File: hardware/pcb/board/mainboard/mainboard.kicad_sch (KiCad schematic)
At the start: 137 parts, among them J1 Conn_Coaxial, J10 USB_C_Receptacle, J11 2908-05WB-MG, J3 Conn_02x35_Odd_Even_MountingP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, J4 Conn_02x40_Odd_Even_MountingP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, J5 Conn_02x40_Odd_Even_MountingP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, J6 USB_C_Receptacle, J7 Conn_01x30, J8 Conn_01x30, J9 Conn_01x30, Q1 BSS138, Q2 DMN3008SFG, Q3 DMN3008SFG, U1 TPS7A20_SOT-23, U11 TPS7A20_SOT-23, U12 AP33771C, U13 TXS0104E, U14 FT234XD-R, U2 LSM6DS3TR, U3 NEO-M8N, U4 BQ25606, U5 BQ27441-G1, U6 SN74LVC1T45DBVR, U7 LIS2MDL, U8 SN74LVC1T45DBVR, U9 TPS61235P

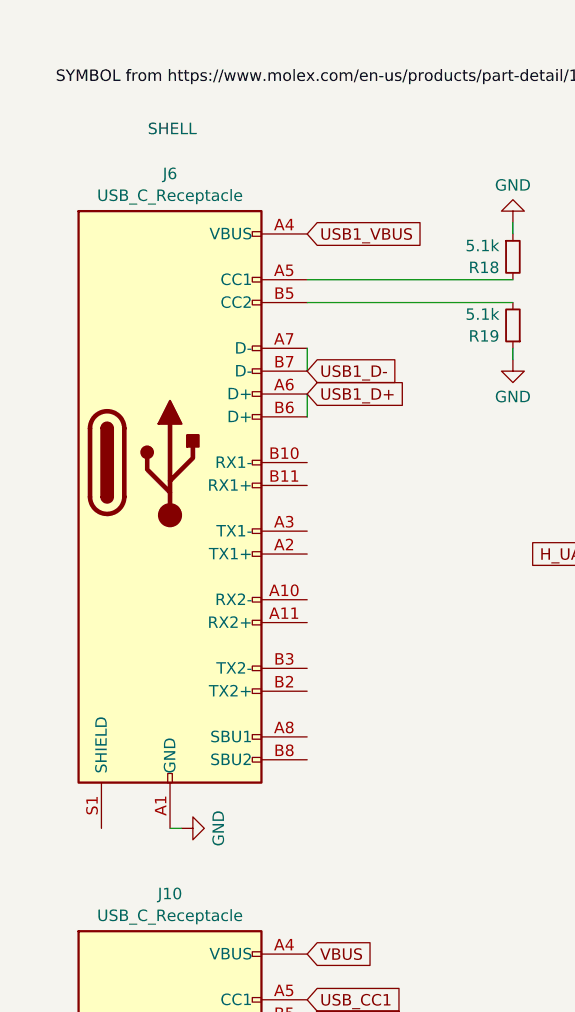
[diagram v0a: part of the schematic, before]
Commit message: switch to vertical USB C receptable for shell
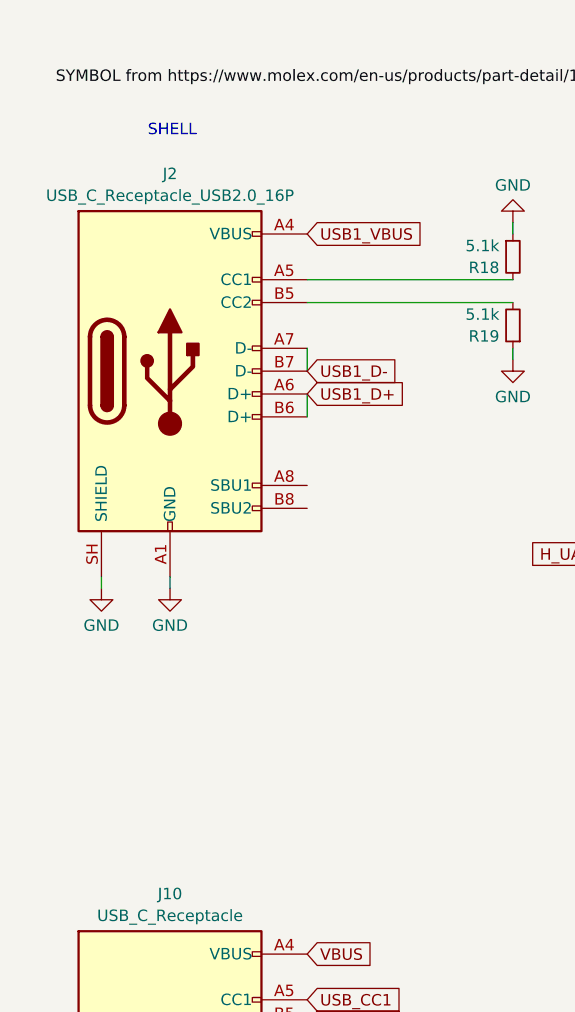
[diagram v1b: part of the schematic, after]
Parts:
- removed J6: USB_C_Receptacle, Connector_USB:USB_C_CONN_1054550101_MOL, symbol Connector:USB_C_Receptacle
- added J2: USB_C_Receptacle_USB2.0_16P, unsurv_offline_pcb_footprints:2171820001_USB_C_MOLEX, symbol Connector:USB_C_Receptacle_USB2.0_16P
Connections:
- net GND: now also J2.A1 (GND), J2.A12 (GND), J2.B1 (GND), J2.B12 (GND), J2.SH (SHIELD)
- net USB1_D+: now also J2.A6 (D+), J2.B6 (D+)
- net USB1_D-: now also J2.A7 (D-), J2.B7 (D-)
- net USB1_VBUS: now also J2.A4 (VBUS), J2.A9 (VBUS), J2.B4 (VBUS), J2.B9 (VBUS)
- net at R19.2: now also J2.B5 (CC2)
- net at R18.2: now also J2.A5 (CC1)
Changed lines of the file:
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@@
 	(wire
 		(pts
+			(xy 31.75 279.4) (xy 31.75 280.67)
+		)
+		(stroke
+			(width 0)
+			(type default)
+		)
+	)
+	(wire
+		(pts
 			(xy 551.18 237.49) (xy 553.72 237.49)
 		)
@@
 	(wire
 		(pts
-			(xy 31.75 307.34) (xy 33.02 307.34)
+			(xy 24.13 279.4) (xy 24.13 280.67)
 		)
 		(stroke
@@
 	)
 	(symbol
-		(lib_id "Connector:USB_C_Receptacle")
-		(at 31.75 266.7 0)
+		(lib_id "Connector:USB_C_Receptacle_USB2.0_16P")
+		(at 31.75 256.54 0)
 		(unit 1)
 		(body_style 1)
@@
 		(dnp no)
 		(fields_autoplaced yes)
-		(property "Reference" "J6"
+		(property "Reference" "J2"
 			(at 31.75 234.6155 0)
 			(show_name no)
@@
 			)
 		)
-		(property "Value" "USB_C_Receptacle"
+		(property "Value" "USB_C_Receptacle_USB2.0_16P"
 			(at 31.75 237.0398 0)
 			(show_name no)
@@
 			)
 		)
-		(property "Footprint" "Connector_USB:USB_C_CONN_1054550101_MOL"
-			(at 35.56 266.7 0)
+		(property "Footprint" "unsurv_offline_pcb_footprints:2171820001_USB_C_MOLEX"
+			(at 35.56 256.54 0)
 			(hide yes)
 			(show_name no)
@@
 		)
 		(property "Datasheet" "https://www.usb.org/sites/default/files/documents/usb_type-c.zip"
-			(at 35.56 266.7 0)
+			(at 35.56 256.54 0)
 			(hide yes)
 			(show_name no)
@@
 			)
 		)
-		(property "Description" "USB Full-Featured Type-C Receptacle connector"
-			(at 31.75 266.7 0)
+		(property "Description" "USB 2.0-only 16P Type-C Receptacle connector"
+			(at 31.75 256.54 0)
 			(hide yes)
 			(show_name no)
@@
 			)
 		)
-		(pin "A5"
-		)
-		(pin "A8"
-		)
-		(pin "B12"
-		)
-		(pin "B1"
+		(pin "A1"
 		)
-		(pin "B3"
+		(pin "A4"
 		)
-		(pin "B8"
+		(pin "A6"
 		)
-		(pin "A4"
+		(pin "B5"
 		)
-		(pin "A2"
+		(pin "B6"
 		)
 		(pin "A7"
 		)
-		(pin "A11"
-		)
-		(pin "A3"
+		(pin "B4"
 		)
-		(pin "B10"
+		(pin "A8"
 		)
-		(pin "B11"
+		(pin "B1"
 		)
-		(pin "A12"
+		(pin "B7"
 		)
 		(pin "B9"
 		)
-		(pin "S1"
-		)
-		(pin "A10"
-		)
-		(pin "B6"
+		(pin "B12"
 		)
-		(pin "A1"
+		(pin "A12"
 		)
-		(pin "B5"
+		(pin "A5"
 		)
 		(pin "A9"
 		)
-		(pin "B2"
-		)
-		(pin "A6"
-		)
-		(pin "B4"
+		(pin "B8"
 		)
-		(pin "B7"
+		(pin "SH"
 		)
 		(instances
 			(project "mainboard"
 				(path "/0d10df44-32de-4e15-8354-02c97578c850"
-					(reference "J6")
+					(reference "J2")
 					(unit 1)
 				)
@@
 	(symbol
 		(lib_id "power:GND")
-		(at 33.02 307.34 90)
+		(at 24.13 280.67 0)
 		(unit 1)
 		(body_style 1)
@@
 		(fields_autoplaced yes)
 		(property "Reference" "#PWR0114"
-			(at 39.37 307.34 0)
+			(at 24.13 287.02 0)
 			(hide yes)
 			(show_name no)
@@
 		)
 		(property "Value" "GND"
-			(at 37.1531 307.34 0)
+			(at 24.13 284.8031 0)
 			(show_name no)
 			(do_not_autoplace no)
@@
 		)
 		(property "Footprint" ""
-			(at 33.02 307.34 0)
+			(at 24.13 280.67 0)
 			(hide yes)
 			(show_name no)
@@
 		)
 		(property "Datasheet" ""
-			(at 33.02 307.34 0)
+			(at 24.13 280.67 0)
 			(hide yes)
 			(show_name no)
@@
 		)
 		(property "Description" "Power symbol creates a global label with name \"GND\" , ground"
-			(at 33.02 307.34 0)
+			(at 24.13 280.67 0)
 			(hide yes)
 			(show_name no)
@@
 					(unit 1)
 				)
+			)
+		)
+	)
+	(symbol
+		(lib_id "power:GND")
+		(at 31.75 280.67 0)
+		(unit 1)
+		(body_style 1)
+		(exclude_from_sim no)
+		(in_bom yes)
+		(on_board yes)
+		(in_pos_files yes)
+		(dnp no)
+		(fields_autoplaced yes)
+		(property "Reference" "#PWR0150"
+			(at 31.75 287.02 0)
+			(hide yes)
+			(show_name no)
+			(do_not_autoplace no)
+			(effects
+				(font
+					(size 1.27 1.27)
+				)
+			)
+		)
+		(property "Value" "GND"
+			(at 31.75 284.8031 0)
+			(show_name no)
+			(do_not_autoplace no)
+			(effects
+				(font
+					(size 1.27 1.27)
+				)
+			)
+		)
+		(property "Footprint" ""
+			(at 31.75 280.67 0)
+			(hide yes)
+			(show_name no)
+			(do_not_autoplace no)
+			(effects
+				(font
+					(size 1.27 1.27)
+				)
+			)
+		)
+		(property "Datasheet" ""
+			(at 31.75 280.67 0)
+			(hide yes)
+			(show_name no)
+			(do_not_autoplace no)
+			(effects
+				(font
+					(size 1.27 1.27)
+				)
+			)
+		)
+		(property "Description" "Power symbol creates a global label with name \"GND\" , ground"
+			(at 31.75 280.67 0)
+			(hide yes)
+			(show_name no)
+			(do_not_autoplace no)
+			(effects
+				(font
+					(size 1.27 1.27)
+				)
+			)
+		)
+		(pin "1"
+		)
+		(instances
+			(project "mainboard"
+				(path "/0d10df44-32de-4e15-8354-02c97578c850"
+					(reference "#PWR0150")
+					(unit 1)
+				)

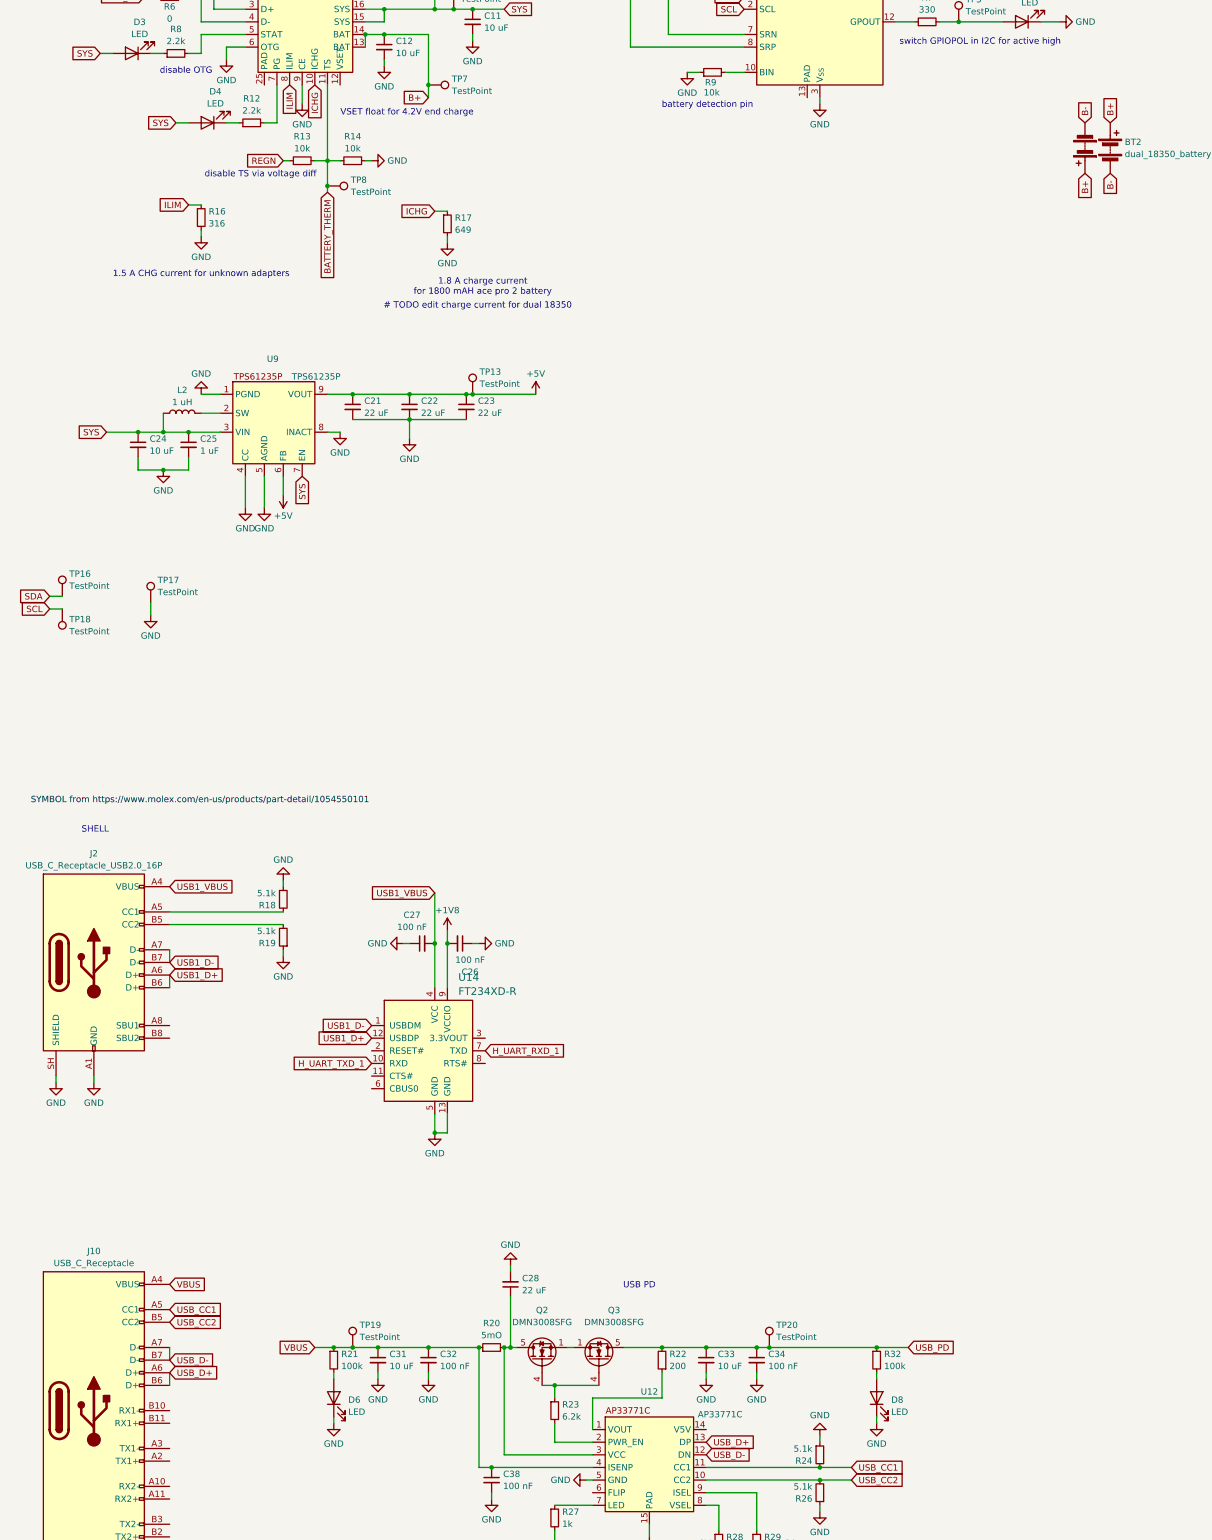
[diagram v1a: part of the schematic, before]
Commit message: BQ25606 routing
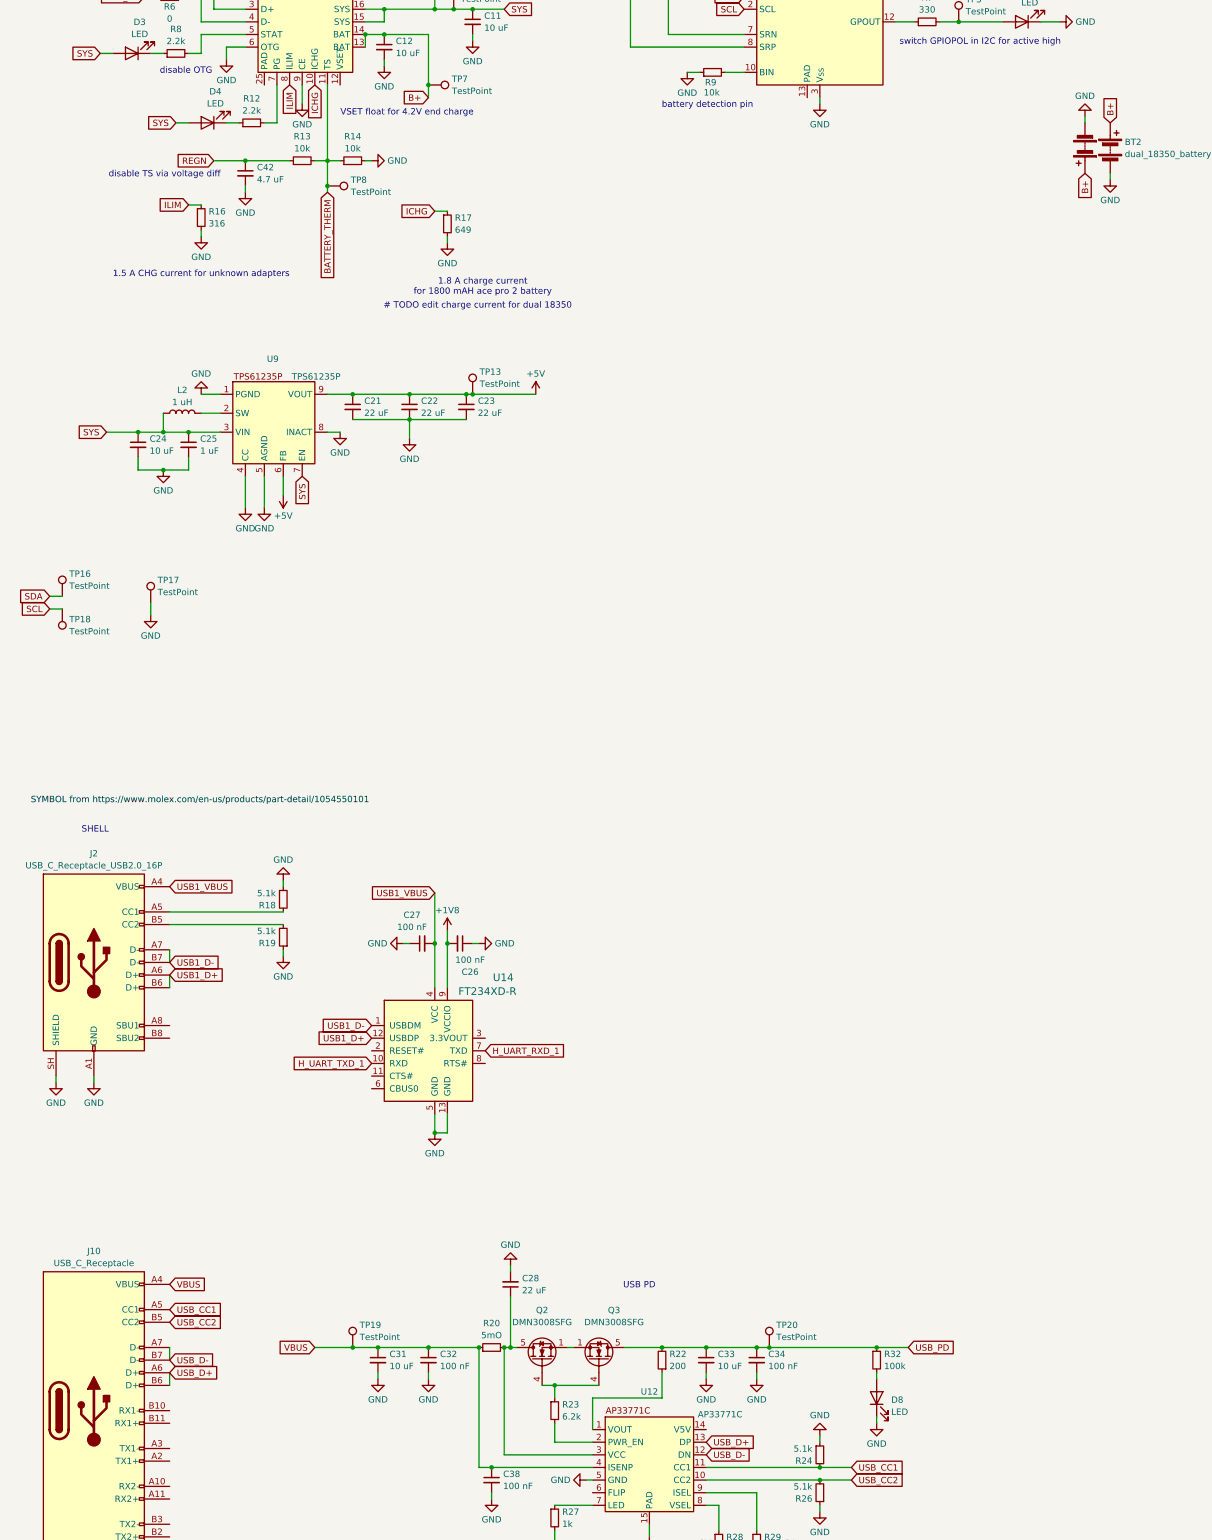
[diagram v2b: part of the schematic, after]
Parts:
- removed D6: LED, LED_SMD:LED_0603_1608Metric, symbol Device:LED
- removed R21: 100k, Resistor_SMD:R_0603_1608Metric, symbol Device:R_Small
- added C42: 4.7 uF, Capacitor_SMD:C_0603_1608Metric, symbol Device:C_Small
- L1: footprint Inductor_SMD:L_0603_1608Metric -> unsurv_offline_pcb_footprints:Inductor_Wuerth_74437321010; MFN (none) -> Wuerth_74437321010
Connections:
- net B- is gone; now on net GND: BT2.2 (-)
- net GND: now also C42.2
- net REGN: now also C42.1

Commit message: TPS61235p 5v PWR routing
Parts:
- L2: footprint Inductor_SMD:L_0603_1608Metric -> Inductor_SMD:L_Coilcraft_XAL5020-XXX; MFN SPM6530T-1R0M120 -> EXLA1V0703-1R0-R
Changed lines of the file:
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@@
 			)
 		)
-		(property "Footprint" "Inductor_SMD:L_0603_1608Metric"
+		(property "Footprint" "Inductor_SMD:L_Coilcraft_XAL5020-XXX"
 			(at 49.53 146.05 0)
 			(hide yes)
@@
 			)
 		)
-		(property "MFN" "SPM6530T-1R0M120"
+		(property "MFN" "EXLA1V0703-1R0-R"
 			(at 49.53 146.05 90)
 			(hide yes)

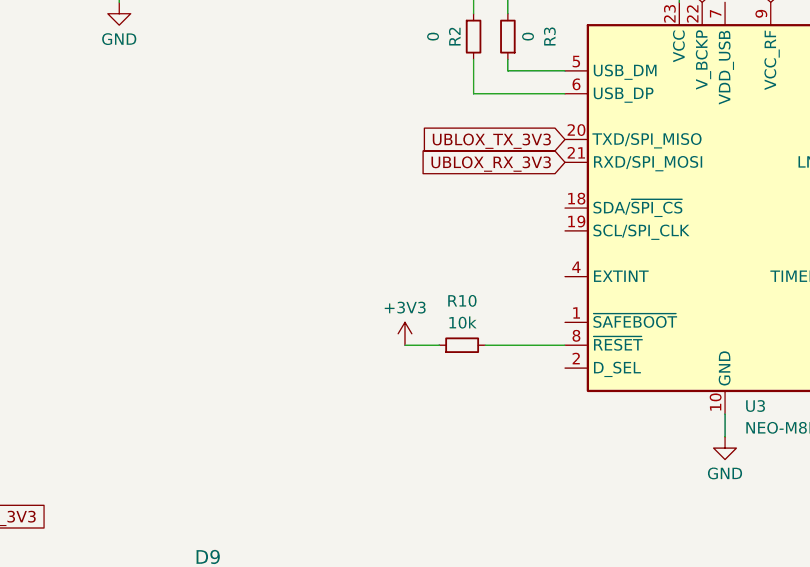
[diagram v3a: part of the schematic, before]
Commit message: route ublox GNSS receiver
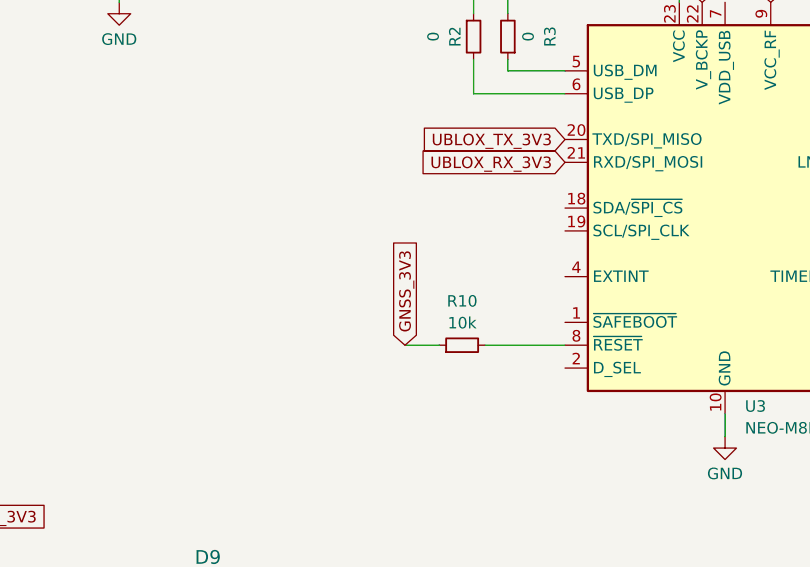
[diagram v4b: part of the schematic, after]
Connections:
- net +3V3: no longer R10.1
- net GNSS_3V3: now also R10.1
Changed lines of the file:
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@@
 		)
 	)
+	(global_label "GNSS_3V3"
+		(shape input)
+		(at 392.43 80.01 90)
+		(fields_autoplaced yes)
+		(effects
+			(font
+				(size 1.27 1.27)
+			)
+			(justify left)
+		)
+		(property "Intersheetrefs" "${INTERSHEET_REFS}"
+			(at 392.43 67.5301 90)
+			(hide yes)
+			(show_name no)
+			(do_not_autoplace no)
+			(effects
+				(font
+					(size 1.27 1.27)
+				)
+				(justify left)
+			)
+		)
+	)
 	(global_label "RX0_2_N"
 		(shape input)
@@
 					(unit 1)
 				)
-			)
-		)
-	)
-	(symbol
-		(lib_id "power:+3V3")
-		(at 392.43 80.01 0)
-		(unit 1)
-		(body_style 1)
-		(exclude_from_sim no)
-		(in_bom yes)
-		(on_board yes)
-		(in_pos_files yes)
-		(dnp no)
-		(fields_autoplaced yes)
-		(property "Reference" "#PWR025"
-			(at 392.43 83.82 0)
-			(hide yes)
-			(show_name no)
-			(do_not_autoplace no)
-			(effects
-				(font
-					(size 1.27 1.27)
-				)
-			)
-		)
-		(property "Value" "+3V3"
-			(at 392.43 75.8769 0)
-			(show_name no)
-			(do_not_autoplace no)
-			(effects
-				(font
-					(size 1.27 1.27)
-				)
-			)
-		)
-		(property "Footprint" ""
-			(at 392.43 80.01 0)
-			(hide yes)
-			(show_name no)
-			(do_not_autoplace no)
-			(effects
-				(font
-					(size 1.27 1.27)
-				)
-			)
-		)
-		(property "Datasheet" ""
-			(at 392.43 80.01 0)
-			(hide yes)
-			(show_name no)
-			(do_not_autoplace no)
-			(effects
-				(font
-					(size 1.27 1.27)
-				)
-			)
-		)
-		(property "Description" "Power symbol creates a global label with name \"+3V3\""
-			(at 392.43 80.01 0)
-			(hide yes)
-			(show_name no)
-			(do_not_autoplace no)
-			(effects
-				(font
-					(size 1.27 1.27)
-				)
-			)
-		)
-		(pin "1"
-		)
-		(instances
-			(project "mainboard"
-				(path "/0d10df44-32de-4e15-8354-02c97578c850"
-					(reference "#PWR025")
-					(unit 1)
-				)
